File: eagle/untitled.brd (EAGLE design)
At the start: 54.8 x 50.8 mm, 29 parts, among them K1 AZ8-FORM-A, Q1 IRFZ24NPBF, U1 ATTINY85-20S, X1 MKDSN1,5/3-5,08, X2 MKDSN1,5/3-5,08

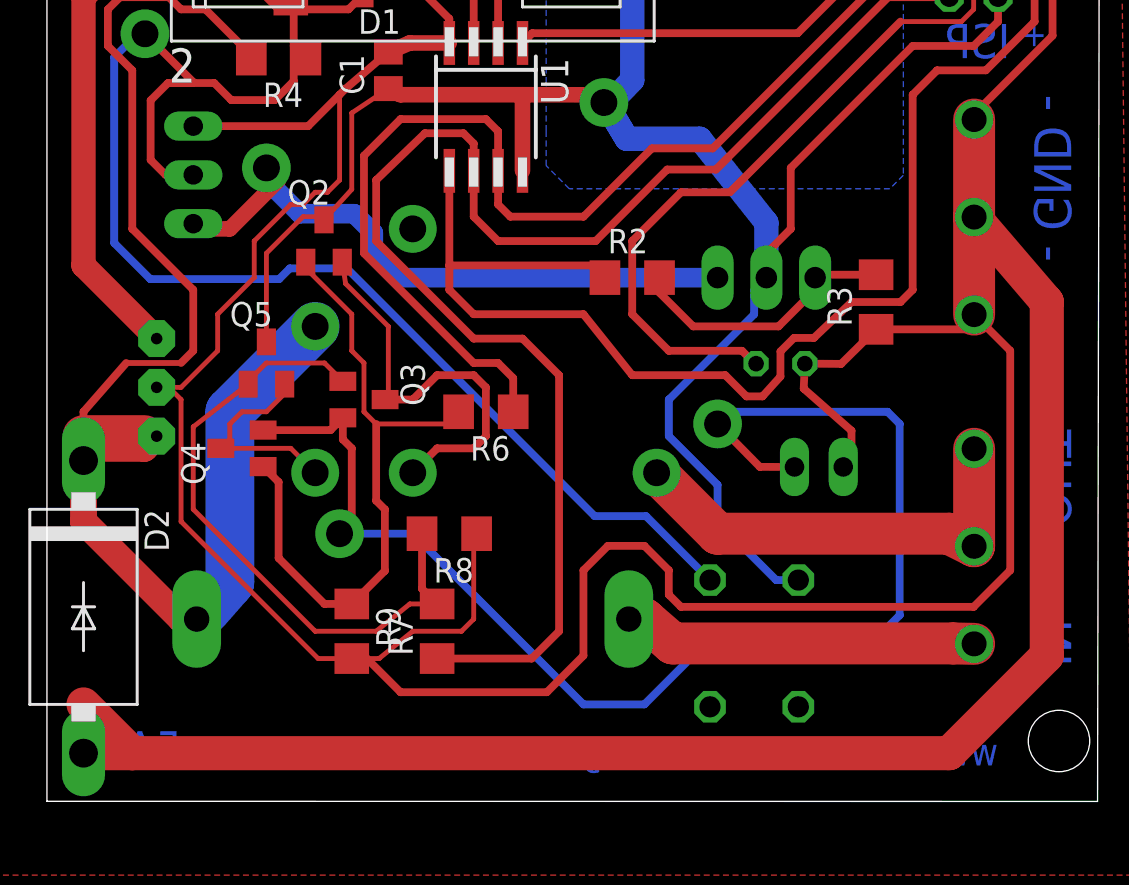
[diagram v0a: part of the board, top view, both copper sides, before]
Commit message: Added resistor for npn transistors
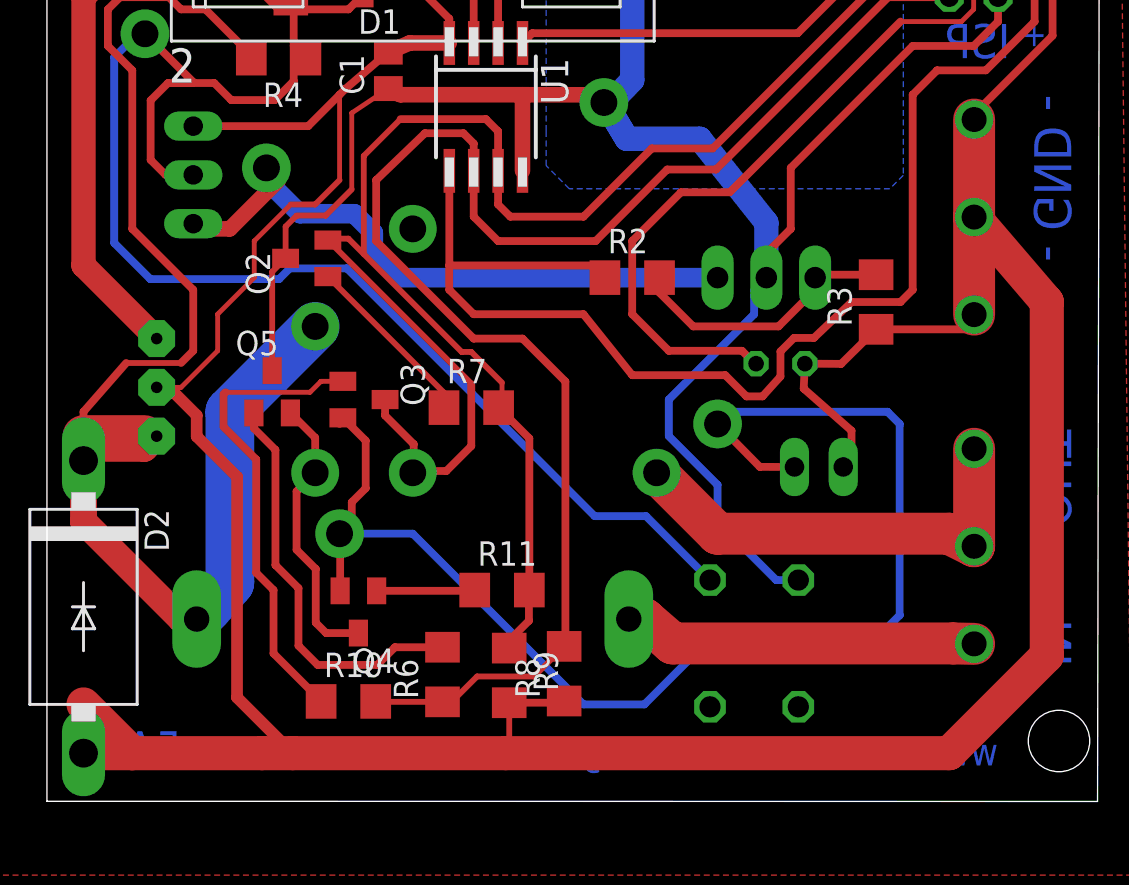
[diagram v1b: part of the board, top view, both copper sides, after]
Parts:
- added R10, R11: 10k, rcl:R1206
- R1: value 1k8 -> 220
- R3: value 10k -> 100k
- R6, R7: value 680 -> 10k
- R8, R9: value 10k -> 200k
- moved R6 13.9 mm to (20.6, 6.00), turned to 90 degrees
- moved R7 11.8 mm to (22.1, 19.9), turned to 0 degrees
- moved Q4 10.5 mm to (16.2, 9.26), turned to 180 degrees
- moved R8 9.43 mm to (26.9, 6.04), turned to 90 degrees
- moved R9 8.52 mm to (24.1, 5.96)
- moved Q5 1.53 mm to (11.7, 20.7)
- moved Q2 1.27 mm to (13.5, 27.7), turned to 90 degrees
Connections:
- removed net N$16: Q3.1, Q5.1, R7.2, R8.2
- removed net N$17: Q2.1, Q4.1, R6.2, R9.1
- new net N$14: Q5.1, R6.2
- new net N$15: Q2.1, R7.1
- new net N$19: Q3.1, R10.1
- new net N$20: Q4.1, R11.1
- net MISO: now also R10.2, R6.1, R8.2; no longer R7.1
- net SCK: now also R11.2, R7.2, R9.1; no longer R6.1
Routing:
- net GND: track 259.5 -> 200.3 mm
- net N$17: track 34.6 -> 0.00 mm
- net N$16: track 33.6 -> 0.00 mm
- net N$19: track 0.00 -> 24.6 mm
- net N$14: track 0.00 -> 21.4 mm
- net SCK: track 59.4 -> 74.8 mm
- net N$15: track 0.00 -> 9.45 mm
- net N$20: track 0.00 -> 5.12 mm
- net MISO: track 76.5 -> 81.6 mm
- net N$13: track 10.9 -> 14.7 mm
- net +5V: track 102.0 -> 103.3 mm
- net N$4: track 71.0 -> 70.1 mm
- net N$11: track 21.3 -> 22.1 mm

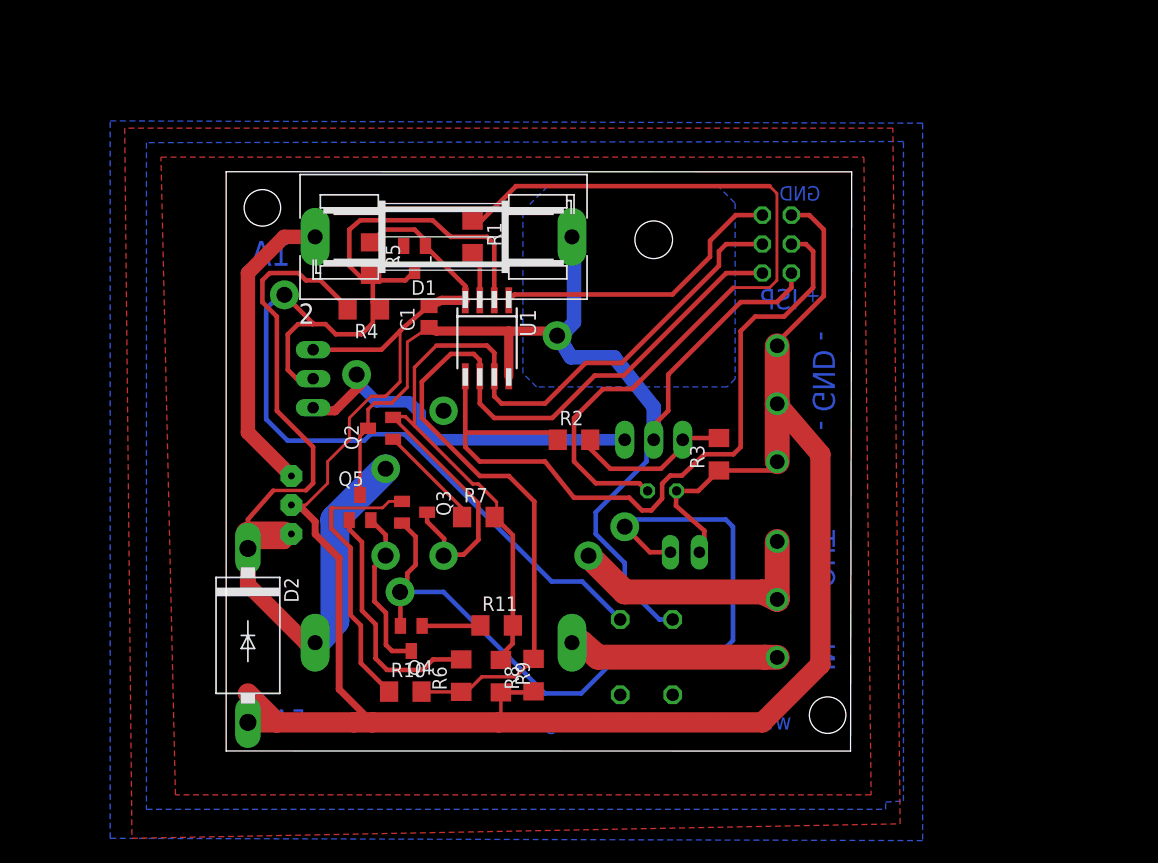
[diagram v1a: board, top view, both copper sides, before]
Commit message: Pullup- reset & 2x voltage divider
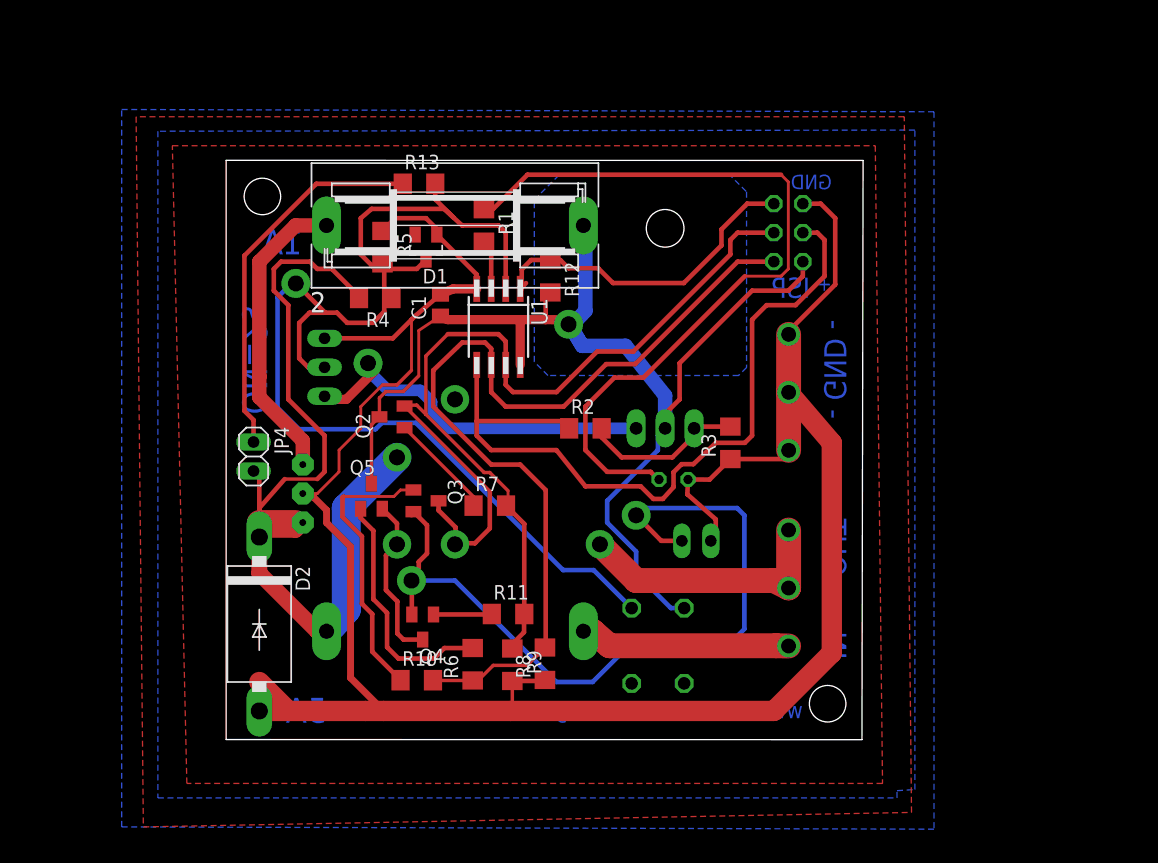
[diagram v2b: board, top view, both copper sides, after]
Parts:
- added JP4: (no value), pinhead:1X02
- added R12: 100k, rcl:R1206
- added R13: 56k, rcl:R1206
- R4: value 10k -> 27k
- moved 1 1.41 mm to (20.1, 9.89)
- moved 2 1.41 mm to (20.1, 45.5)
- moved C1 1.41 mm to (18.8, 38.5)
- moved D1 1.41 mm to (17.5, 43.5)
- moved JP2 1.41 mm to (49.3, 44.8)
- moved JP3 1.41 mm to (41.2, 17.8)
- moved K1 1.41 mm to (23.9, 23.9)
- moved LED1 1.41 mm to (39.2, 23.2)
- moved Q1 1.41 mm to (38.5, 34.0)
- moved Q2 1.41 mm to (14.5, 28.7)
- moved Q3 1.41 mm to (17.5, 21.3)
- moved Q4 1.41 mm to (17.2, 10.3)
- moved Q5 1.41 mm to (12.7, 21.7)
- moved R1 1.41 mm to (22.6, 45.5)
- moved R10 1.41 mm to (16.7, 5.60)
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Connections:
- new net N$16: JP4.1, R13.1
- net +5V: now also R12.2
- net N$10: now also R12.1
- net N$2: now also JP4.2
- net RESET: now also R13.2
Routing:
- net N$16: track 0.00 -> 33.1 mm
- net N$2: track 75.4 -> 81.7 mm
- net N$3: track 28.1 -> 23.1 mm
- net RESET: track 102.1 -> 105.7 mm
- net N$10: track 26.1 -> 29.5 mm
- net +5V: track 103.3 -> 105.8 mm
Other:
- board size 54.8 x 50.8 mm -> 55.8 x 50.8 mm
- board text added: "ON=2s"
- board text added: "www.tief-dunkel-kalt.org 01/16 V1.2"
- board text removed: "www.tief-dunkel-kalt.org 01/16 V1.1"

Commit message: Additional jumper for 2s and 3s lipo battery
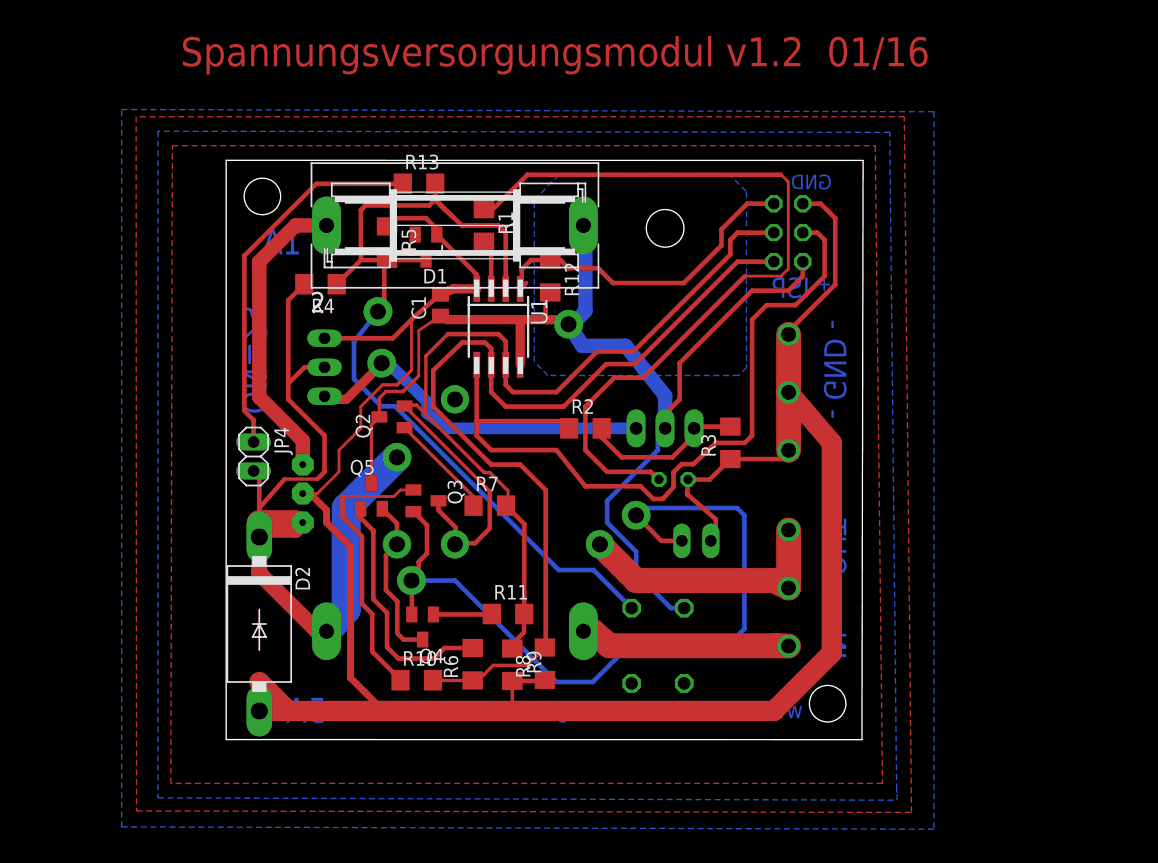
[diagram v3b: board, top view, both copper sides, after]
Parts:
- moved R4 4.95 mm to (8.27, 40.3)
- moved R5 0.57 mm to (14.1, 43.9)
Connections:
- net N$2: now also JP1.2
- net RESET: no longer JP1.2
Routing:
- net RESET: track 105.7 -> 80.9 mm
- net N$2: track 81.7 -> 74.3 mm
- net GND: track 200.3 -> 199.8 mm
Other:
- board text added: "Spannungsversorgungsmodul v1.2 01/16"

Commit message: Changed relais. Fixed compiler failures
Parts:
- removed K1: AZ8-FORM-A, 0liver:AZ8
- added U$2: TRS-1BISTABIL-SCHRACK, 0liver:PRINTRELAIS-SCHRACK-PE-BISTABIL
- D1: value 5.1V -> 4.7V
- R13: value 56k -> 1,5k
- R4: value 27k -> 1,8k
- R5: value 10k -> 1k
- moved R2 0.80 mm to (30.7, 27.7)
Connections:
- removed net N$3: K1.1, X1.2, X1.3
- new net N$17: U$2.P$4, X1.2, X1.3
- net N$11: now also U$2.P$1; no longer K1.2
- net N$13: now also U$2.P$2; no longer K1.5
- net N$2: now also U$2.P$3; no longer K1.3
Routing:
- net N$17: track 0.00 -> 23.2 mm
- net N$3: track 23.1 -> 0.00 mm
- net N$2: track 74.3 -> 85.3 mm, vias 0 -> 1
- net N$11: track 22.1 -> 28.1 mm
- net MOSI: track 67.7 -> 63.0 mm
- net N$6: track 69.9 -> 73.2 mm
- net RESET: track 80.9 -> 83.6 mm
- net SCK: track 74.8 -> 76.9 mm
- net MISO: track 81.6 -> 82.5 mm
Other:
- board text added: "Spannungsversorgungsmodul v1.3 01/16"
- board text added: "www.tief-dunkel-kalt.org 01/16 V1.3"
- board text removed: "Spannungsversorgungsmodul v1.2 01/16"
- board text removed: "www.tief-dunkel-kalt.org 01/16 V1.2"

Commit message: Lots of essential changes to functionality
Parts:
- R10, R11, R6, R7: value 10k -> 6,8k
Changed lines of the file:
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@@
 <element name="D1" library="diode" package="SOT23" value="4.7V" x="17.51" y="43.545" rot="R180"/>
 <element name="D2" library="diode" package="DO201-15" value="" x="2.905" y="10.525" rot="R270"/>
-<element name="R6" library="rcl" package="R1206" value="10k" x="21.6" y="7" rot="R90"/>
-<element name="R7" library="rcl" package="R1206" value="10k" x="23.1" y="20.9"/>
-<element name="R10" library="rcl" package="R1206" value="10k" x="16.7" y="5.6"/>
-<element name="R11" library="rcl" package="R1206" value="10k" x="24.7" y="11.4"/>
+<element name="R6" library="rcl" package="R1206" value="6,8k" x="21.6" y="7" rot="R90"/>
+<element name="R7" library="rcl" package="R1206" value="6,8k" x="23.1" y="20.9"/>
+<element name="R10" library="rcl" package="R1206" value="6,8k" x="16.7" y="5.6"/>
+<element name="R11" library="rcl" package="R1206" value="6,8k" x="24.7" y="11.4"/>
 <element name="R12" library="rcl" package="R1206" value="100k" x="28.4" y="41" rot="R270"/>
 <element name="JP4" library="pinhead" package="1X02" value="" x="2.4" y="25.2" rot="R270"/>
